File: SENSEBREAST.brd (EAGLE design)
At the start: 64 x 56 mm, 16 parts, among them IC1 BME280, IC2 MCP3202SN, IC3 LSM9DS1, J1 M40-SOCKET-BELOW, J2 Heart Rate

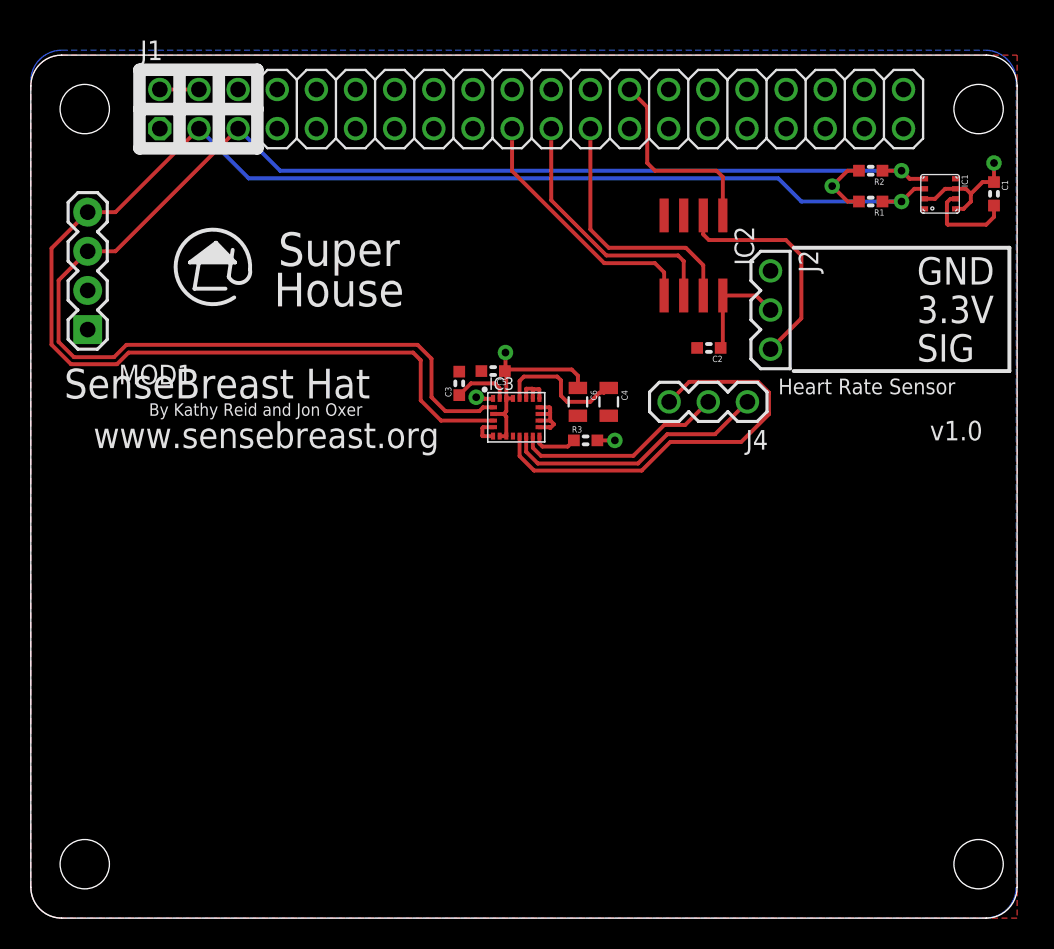
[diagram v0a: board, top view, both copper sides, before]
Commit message: Replaced BME280 with BME680 to allow detection of VOC levels in the environment
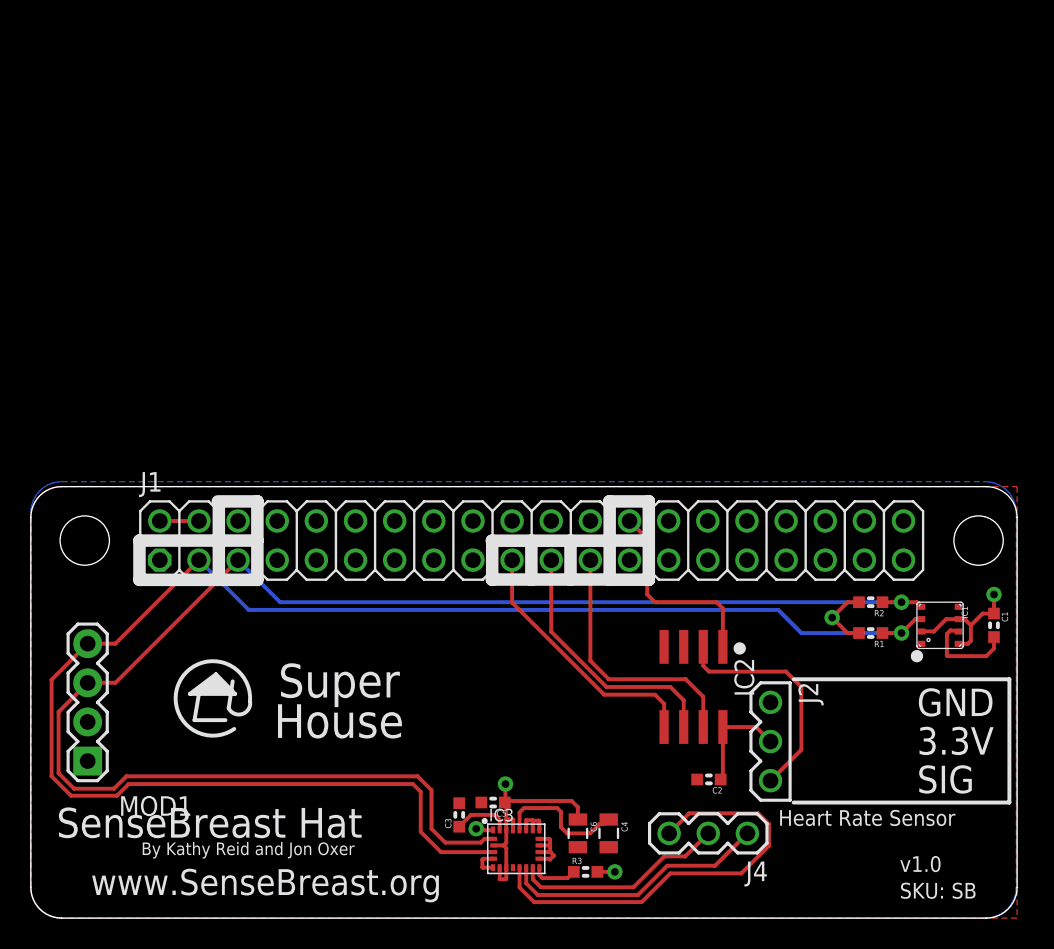
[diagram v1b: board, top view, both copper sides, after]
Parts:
- IC1: value BME280 -> BME680; device SuperHouse-Sensors:BME280 -> SuperHouse-Sensors:BME680
- J4: value (none) -> INTERRUPTS
- moved C3 28.0 mm to (27.8, 6.70)
- moved C1 28.0 mm to (62.5, 19.0)
- moved C2 28.0 mm to (44.0, 9.00)
- moved C4 28.0 mm to (37.5, 5.50)
- moved C5 28.0 mm to (30.0, 7.50)
- moved C6 28.0 mm to (35.5, 5.50)
- moved IC1 28.0 mm to (59.0, 19.0)
- moved IC2 28.0 mm to (43.0, 15.0)
- moved IC3 28.0 mm to (31.5, 4.50)
- moved J2 28.0 mm to (48.0, 14.0)
- moved J4 28.0 mm to (46.5, 5.50)
- moved MOD1 28.0 mm to (23.0, 14.0)
- moved R1 28.0 mm to (54.5, 18.5)
- moved R2 28.0 mm to (54.5, 20.5)
- moved R3 28.0 mm to (36.0, 3.00)
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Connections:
- net N$2 renamed INT1_A
- net N$3 renamed INT2_A
- net N$5 renamed INT_M
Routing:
- net 3.3V: track 34.5 -> 37.1 mm
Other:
- board size 64 x 56 mm -> 64 x 28 mm
- board text added: "INT1"
- board text added: "INT2"
- board text added: "INTM"
- board text added: "MCP3202SN SPI CS: GPIO7 BME680 temp / humid: 0x76 LSM9DS1 magnetometer: 0x1C LSM9DS1 accel/gyro: 0x6A SSD1306 OLED: 0x3C"
- board text added: "SCL"
- board text added: "SDA"
- board text added: "SKU: SB"
- board text added: "www.SenseBreast.org"
- board text removed: "I2C Addresses 0x??: BME280 0x3C: SSD1306 128x32 OLED"
- board text removed: "www.sensebreast.org"

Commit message: Final routing, plus ERC and DRC for v1.0 release
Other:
- board text added: "SKU: SENSEBREAST"
- board text removed: "SKU: SB"
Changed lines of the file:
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@@
 <text x="1.665" y="5.22" size="1.9304" layer="21" font="vector" ratio="15">SenseBreast Hat</text>
 <text x="7.165" y="4.5" size="0.8128" layer="21" font="vector" ratio="15" distance="30" align="center-left">By Kathy Reid and Jon Oxer</text>
-<text x="56.38" y="3" size="1.016" layer="21" font="vector" ratio="15">v1.0</text>
+<text x="48.88" y="3" size="1.016" layer="21" font="vector" ratio="15">v1.0</text>
 <text x="15.28" y="1.5" size="1.6764" layer="21" font="vector" ratio="15" align="bottom-center">www.SenseBreast.org</text>
 <text x="20" y="16.5" size="2.1844" layer="21" font="vector" ratio="16" distance="20" align="top-center">Super
@@
 <wire x1="37.53" y1="24.5" x2="40.1" y2="24.5" width="0.8128" layer="21"/>
 <wire x1="12.13" y1="27.04" x2="14.7" y2="27.04" width="0.8128" layer="21"/>
-<text x="56.38" y="1.27" size="1.016" layer="21" font="vector" ratio="16" distance="20">SKU: SB</text>
+<text x="48.88" y="1.27" size="1.016" layer="21" font="vector" ratio="16" distance="20">SKU: SENSEBREAST</text>
 <text x="5.52" y="17.78" size="1.27" layer="22" font="vector" ratio="16" distance="20" rot="MR0" align="center-right">SDA</text>
 <text x="5.52" y="15.24" size="1.27" layer="22" font="vector" ratio="16" distance="20" rot="MR0" align="center-right">SCL</text>
